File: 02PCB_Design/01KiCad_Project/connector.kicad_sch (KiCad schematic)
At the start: 7 parts, among them J5 DE9_Receptacle_MountingHoles, J6 MTSW-104-22-L-D-265-RA, J7 Conn_01x06_Pin

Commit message: Layout progress
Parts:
- J5: footprint (none) -> Connector_Dsub:DSUB-9_Female_Horizontal_P2.77x2.84mm_EdgePinOffset4.94mm_Housed_MountingHolesOffset7.48mm
- J6: footprint (none) -> Connector_PinHeader_2.54mm:PinHeader_2x04_P2.54mm_Horizontal
- J7: footprint (none) -> Connector_PinHeader_2.54mm:PinHeader_2x03_P2.54mm_Horizontal
- U12: value ~ -> MCP2562FD; footprint (none) -> Package_SO:SOIC-8_3.9x4.9mm_P1.27mm
- renumbered C69 to C70, C70 to C71, R47 to R46
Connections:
- net +3.3V: now also J6.6 (06), J7.4 (Pin_4), U12.5 (VIO); no longer J6.05, J7.5 (Pin_5), U12. (VSS)
- net +5V: now also U12.3 (VDD); no longer U12. (VSS)
- net ENC_CS: now also J6.3 (03); no longer J6.03
- net FDCAN_RX: now also U12.4 (RXD); no longer U12. (VSS)
- net FDCAN_TX: now also U12.1 (TXD); no longer U12. (VSS)
- net GNDA: now also J6.7 (07), J7.2 (Pin_2), U12.2 (VSS), U12.8 (STBY); no longer J6.01, J7.1 (Pin_1), U12. (VSS)
- net IMU_CS: now also J6.4 (04); no longer J6.04
- net IMU_INT1: now also J6.8 (08); no longer J6.08
- net O_ENC_A: now also J7.1 (Pin_1); no longer J7.2 (Pin_2)
- net O_ENC_B: now also J7.5 (Pin_5); no longer J7.3 (Pin_3)
- net O_ENC_I: now also J7.3 (Pin_3); no longer J7.4 (Pin_4)
- net SPI_MISO: now also J6.5 (05); no longer J6.06
- net SPI_MOSI: now also J6.2 (02); no longer J6.07
- net SPI_SCLK: now also J6.1 (01); no longer J6.02
- net at J5.7, R46.1: now also U12.7 (CANH); no longer U12. (VSS)
- net at J5.2, R46.2: now also U12.6 (CANL); no longer U12. (VSS)

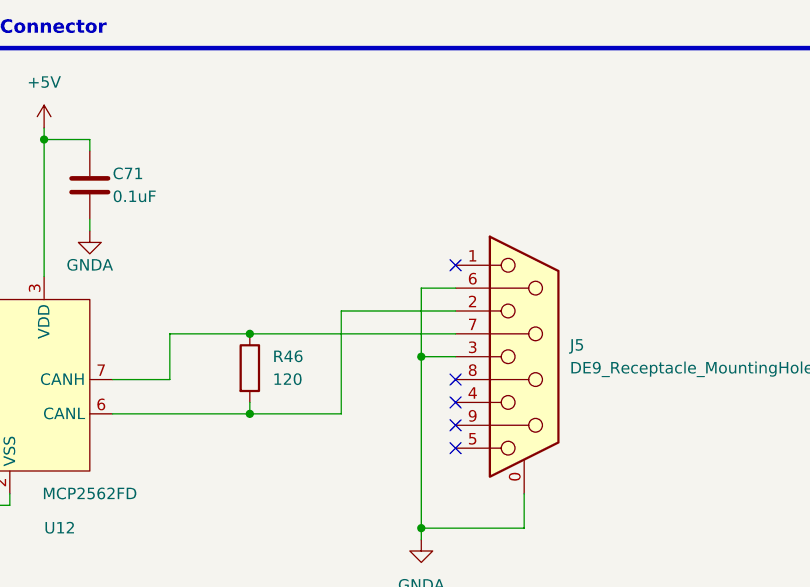
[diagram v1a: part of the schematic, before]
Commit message: routed signals
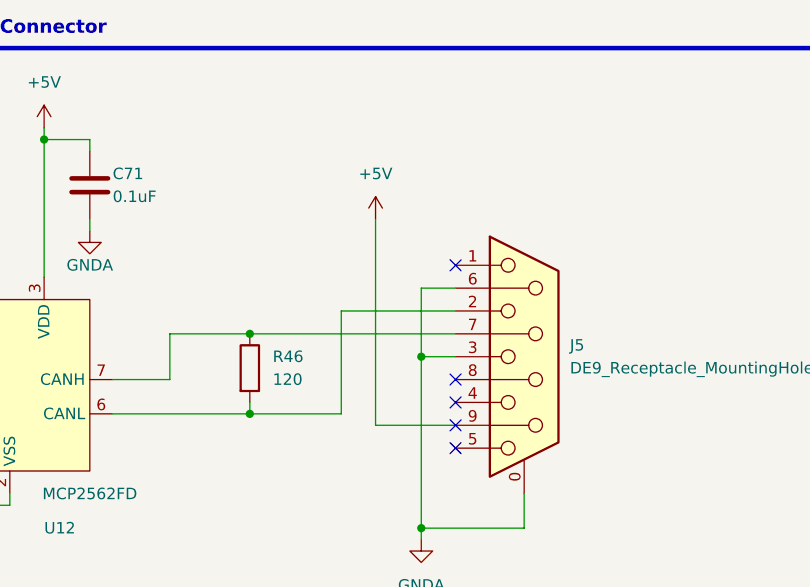
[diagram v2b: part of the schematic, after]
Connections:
- net +5V: now also J5.9
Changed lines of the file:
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@@
+    (stroke (width 0) (type default))
+  )
+  (wire (pts (xy 152.4 82.55) (xy 161.29 82.55))
     (stroke (width 0) (type default))
   )
@@
   )
   (wire (pts (xy 172.72 123.19) (xy 172.72 125.73))
+    (stroke (width 0) (type default))
+  )
+  (wire (pts (xy 152.4 59.69) (xy 152.4 82.55))
     (stroke (width 0) (type default))
   )
@@
         )
       )
+    )
+  )
+  (symbol (lib_id "power:+5V") (at 152.4 59.69 0) (unit 1)
+    (in_bom yes) (on_board yes) (dnp no) (fields_autoplaced)
+    (property "Reference" "#PWR081" (at 152.4 63.5 0)
+      (effects (font (size 1.27 1.27)) hide)
+    )
+    (property "Value" "+5V" (at 152.4 54.61 0)
+      (effects (font (size 1.27 1.27)))
+    )
+    (property "Footprint" "" (at 152.4 59.69 0)
+      (effects (font (size 1.27 1.27)) hide)
+    )
+    (property "Datasheet" "" (at 152.4 59.69 0)
+      (effects (font (size 1.27 1.27)) hide)
+    )
+    (pin "1")
+    (instances
+      (project "Testplatine"
+        (path "/de27a806-41f8-462d-8678-2476d523bbd9/a9fc49c7-f356-4c2b-bdd5-d12f8bcc20f7/71441778-19c6-49de-8dce-f1083f9dacbc"
+          (reference "#PWR081") (unit 1)
+        )
+      )

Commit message: Design 1.0 Finished
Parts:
- renumbered R46 to R42
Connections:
- net +3.3V: now also J5.9
- net +5V: no longer J5.9
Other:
- moved on the sheet: J6, J7
